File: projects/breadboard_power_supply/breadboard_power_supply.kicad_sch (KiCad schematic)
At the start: 17 parts, among them J1 Barrel_Jack_Switch, J2 Conn_01x03_Pin, J3 Conn_01x02_Pin, J4 Screw_Terminal_01x02, J5 Conn_01x03_Pin, J6 Screw_Terminal_01x02, J7 Conn_01x02_Pin, U1 LM317_TO-220, U2 LM7805_TO220

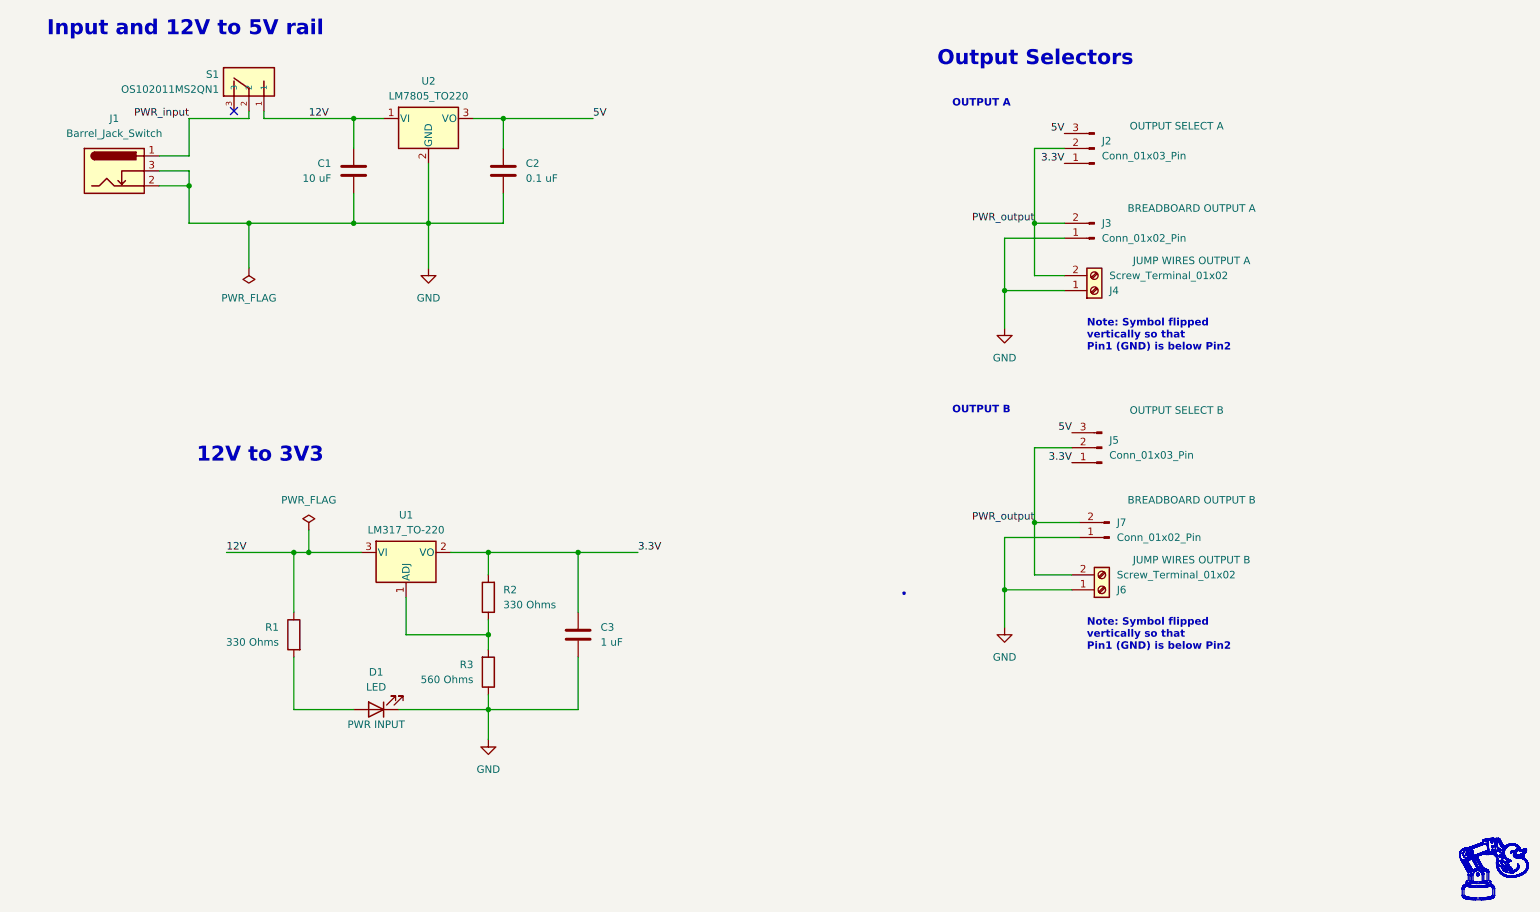
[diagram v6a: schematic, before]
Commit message: Finish breadboard_power_supply projeect in v1
Finish PCB design
Correct design issues in schematic and PCB: separate power_output nets A and B,
rewire accordingly
Add silkscreen text and decorations
Improve 3D
Improve notes
Add figures
Generate gerbers
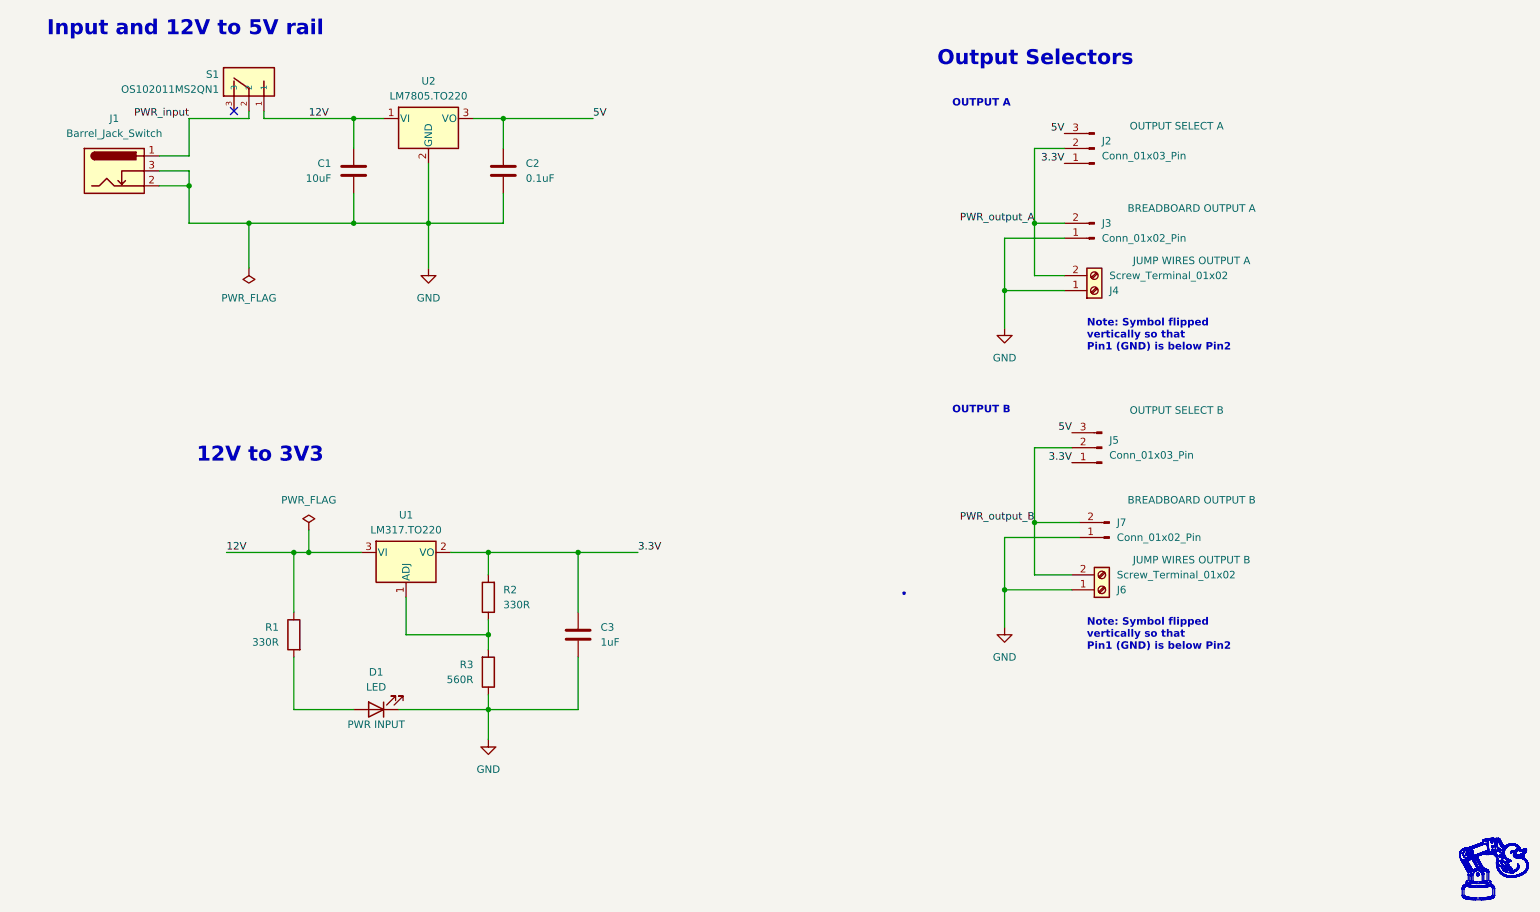
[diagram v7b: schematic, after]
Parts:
- C1: value 10 uF -> 10uF
- C2: value 0.1 uF -> 0.1uF
- C3: value 1 uF -> 1uF
- J2, J5: footprint Connector_PinHeader_2.54mm:PinHeader_1x03_P2.54mm_Horizontal -> Connector_PinHeader_2.54mm:PinHeader_1x03_P2.54mm_Vertical
- R1, R2: value 330 Ohms -> 330R
- R3: value 560 Ohms -> 560R
- U1: value LM317_TO-220 -> LM317.TO220
- U2: value LM7805_TO220 -> LM7805.TO220
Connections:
- net PWR_output renamed PWR_output_A
- net PWR_output_A: no longer J5.2 (Pin_2), J6.2 (Pin_2), J7.2 (Pin_2)
- new net PWR_output_B: J5.2 (Pin_2), J6.2 (Pin_2), J7.2 (Pin_2)
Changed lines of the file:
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@@
 		)
 		(fill
-			(type outline)
+			(type color)
+			(color 0 0 0 0)
 		)
 	)
@@
 		)
 		(fill
-			(type outline)
+			(type color)
+			(color 0 0 0 0)
 		)
 	)
@@
 		)
 		(fill
-			(type outline)
+			(type color)
+			(color 0 0 0 0)
 		)
 	)
@@
 		)
 		(fill
-			(type outline)
+			(type color)
+			(color 0 0 0 0)
 		)
 	)
@@
 		)
 		(fill
-			(type outline)
+			(type color)
+			(color 0 0 0 0)
 		)
 	)
@@
 		)
 		(fill
-			(type outline)
+			(type color)
+			(color 0 0 0 0)
 		)
 	)
@@
 		)
 		(fill
-			(type outline)
+			(type color)
+			(color 0 0 0 0)
 		)
 	)
@@
 		)
 		(fill
-			(type outline)
+			(type color)
+			(color 0 0 0 0)
 		)
 	)
@@
 		)
 		(fill
-			(type outline)
+			(type color)
+			(color 0 0 0 0)
 		)
 	)
@@
 		)
 		(fill
-			(type outline)
+			(type color)
+			(color 0 0 0 0)
 		)
 	)
@@
 		)
 		(fill
-			(type outline)
+			(type color)
+			(color 0 0 0 0)
 		)
 	)
@@
 		)
 		(fill
-			(type outline)
+			(type color)
+			(color 0 0 0 0)
 		)
 	)
@@
 		)
 		(fill
-			(type outline)
+			(type color)
+			(color 0 0 0 0)
 		)
 	)
@@
 		)
 		(fill
-			(type outline)
+			(type color)
+			(color 0 0 0 0)
 		)
 	)
@@
 		)
 	)
-	(label "PWR_output"
+	(label "PWR_output_B"
 		(at 198.12 115.57 180)
 		(effects
@@
 		)
 	)
+	(label "PWR_output_A"
+		(at 198.12 64.77 180)
+		(effects
+			(font
+				(size 1.27 1.27)
+			)
+			(justify right bottom)
+		)
+	)
 	(label "3.3V"
 		(at 130.81 120.65 0)
@@
 		)
 	)
-	(label "PWR_output"
-		(at 198.12 64.77 180)
-		(effects
-			(font
-				(size 1.27 1.27)
-			)
-			(justify right bottom)
-		)
-	)
 	(label "12V"
 		(at 60.96 120.65 0)
@@
 			)
 		)
-		(property "Value" "10 uF"
+		(property "Value" "10uF"
 			(at 78.74 57.1499 0)
 			(effects
@@
 			)
 		)
-		(property "Footprint" "Connector_PinHeader_2.54mm:PinHeader_1x03_P2.54mm_Horizontal"
+		(property "Footprint" "Connector_PinHeader_2.54mm:PinHeader_1x03_P2.54mm_Vertical"
 			(at 209.55 102.87 0)
 			(effects
@@
 			)
 		)
-		(property "Footprint" "Connector_PinHeader_2.54mm:PinHeader_1x03_P2.54mm_Horizontal"
+		(property "Footprint" "Connector_PinHeader_2.54mm:PinHeader_1x03_P2.54mm_Vertical"
 			(at 208.28 52.07 0)
 			(effects
@@
 			)
 		)
-		(property "Value" "LM7805_TO220"
+		(property "Value" "LM7805.TO220"
 			(at 95.25 43.18 0)
 			(effects
@@
 			)
 		)
-		(property "Value" "330 Ohms"
+		(property "Value" "330R"
 			(at 107.95 129.5399 0)
 			(effects
@@
 			)
 		)
-		(property "Value" "330 Ohms"
+		(property "Value" "330R"
 			(at 69.85 135.8899 0)
 			(effects
@@
 			)
 		)
-		(property "Value" "0.1 uF"
+		(property "Value" "0.1uF"
 			(at 111.76 57.1499 0)
 			(effects
@@
 			)
 		)
-		(property "Value" "560 Ohms"
+		(property "Value" "560R"
 			(at 102.87 142.2399 0)
 			(effects
@@
 			)
 		)
-		(property "Value" "LM317_TO-220"
+		(property "Value" "LM317.TO220"
 			(at 91.44 116.84 0)
 			(effects
@@
 			)
 		)
-		(property "Value" "1 uF"
+		(property "Value" "1uF"
 			(at 124.46 135.8899 0)
 			(effects

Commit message: breadboard power supply version v2.0
Changes in v2.0 (Dec'25):

- fix errors:
  - flip Switch S1 (so OFF and ON work as intended)
  - flip J4 Screw Terminal (so vA+ and vA- are as intended)

- update schematics:
  - improve readability
  - update version number to v2.0

- update silkscreen:
  - Update version number in back silkscreen to v2.0
  - fix footprint of J4 screw terminal in front silkscreen

- update 3D view:
  - color mask black
  - add jumpers

Update text and figures in README.md
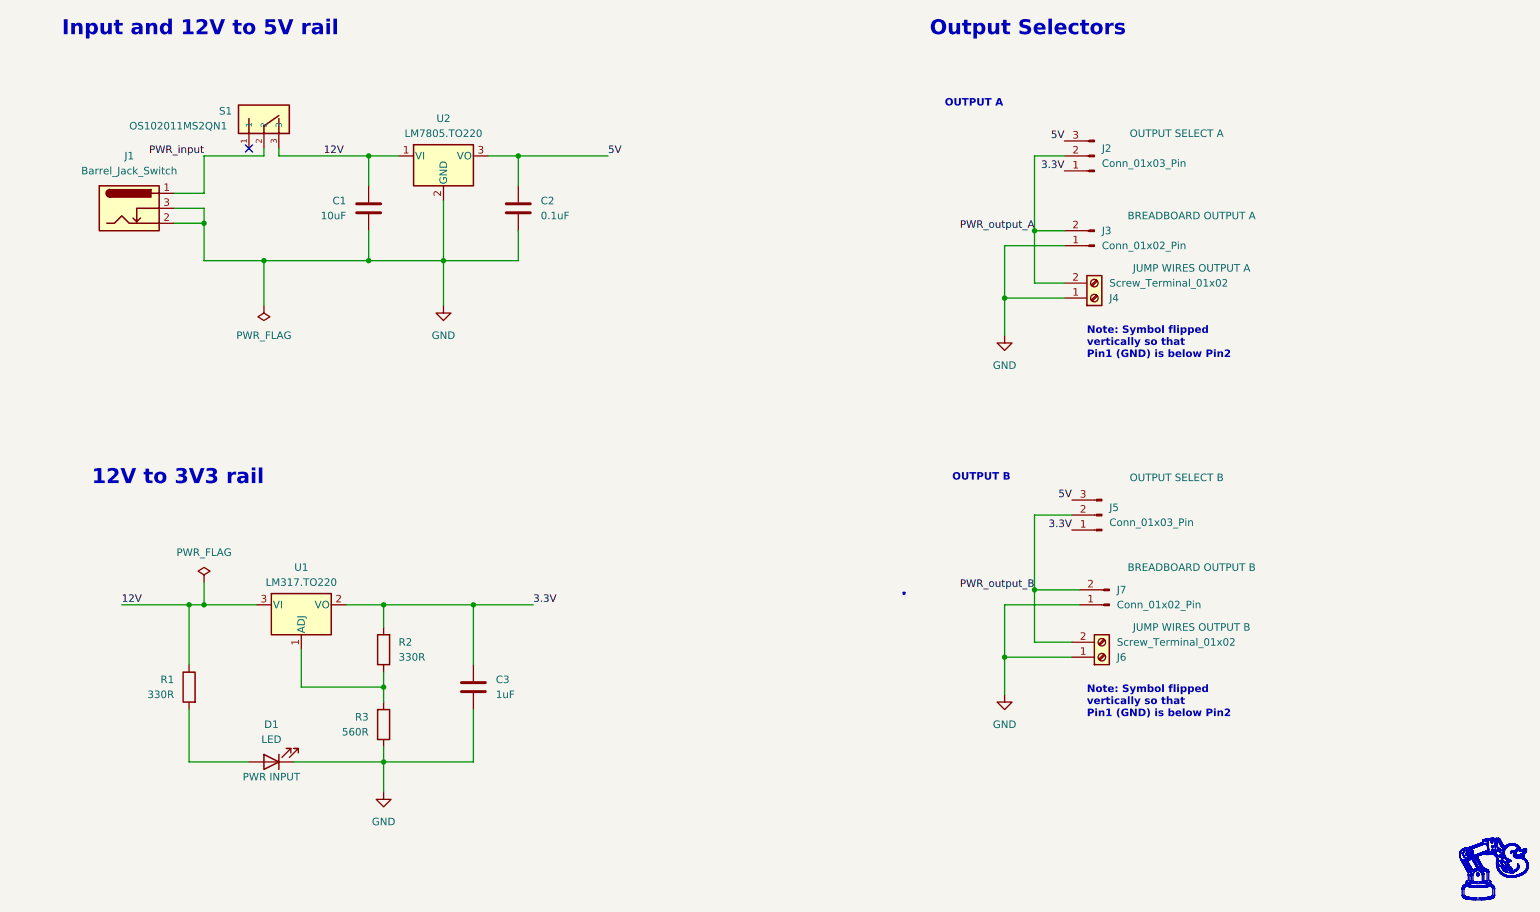
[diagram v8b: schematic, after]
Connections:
- net 12V: now also S1.3; no longer S1.1
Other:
- note added: "12V to 3V3 rail"
- note removed: "12V to 3V3"
- moved on the sheet: C1, C2, C3, D1, J1, J2, J3, J4, J5, J6, J7, R1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
